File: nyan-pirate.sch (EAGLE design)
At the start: 40 parts, among them IC1 PIC24FJ64GA002, IC2 FT232RL, IC3 4066, J1 CON-USB-MINI-BUSB1

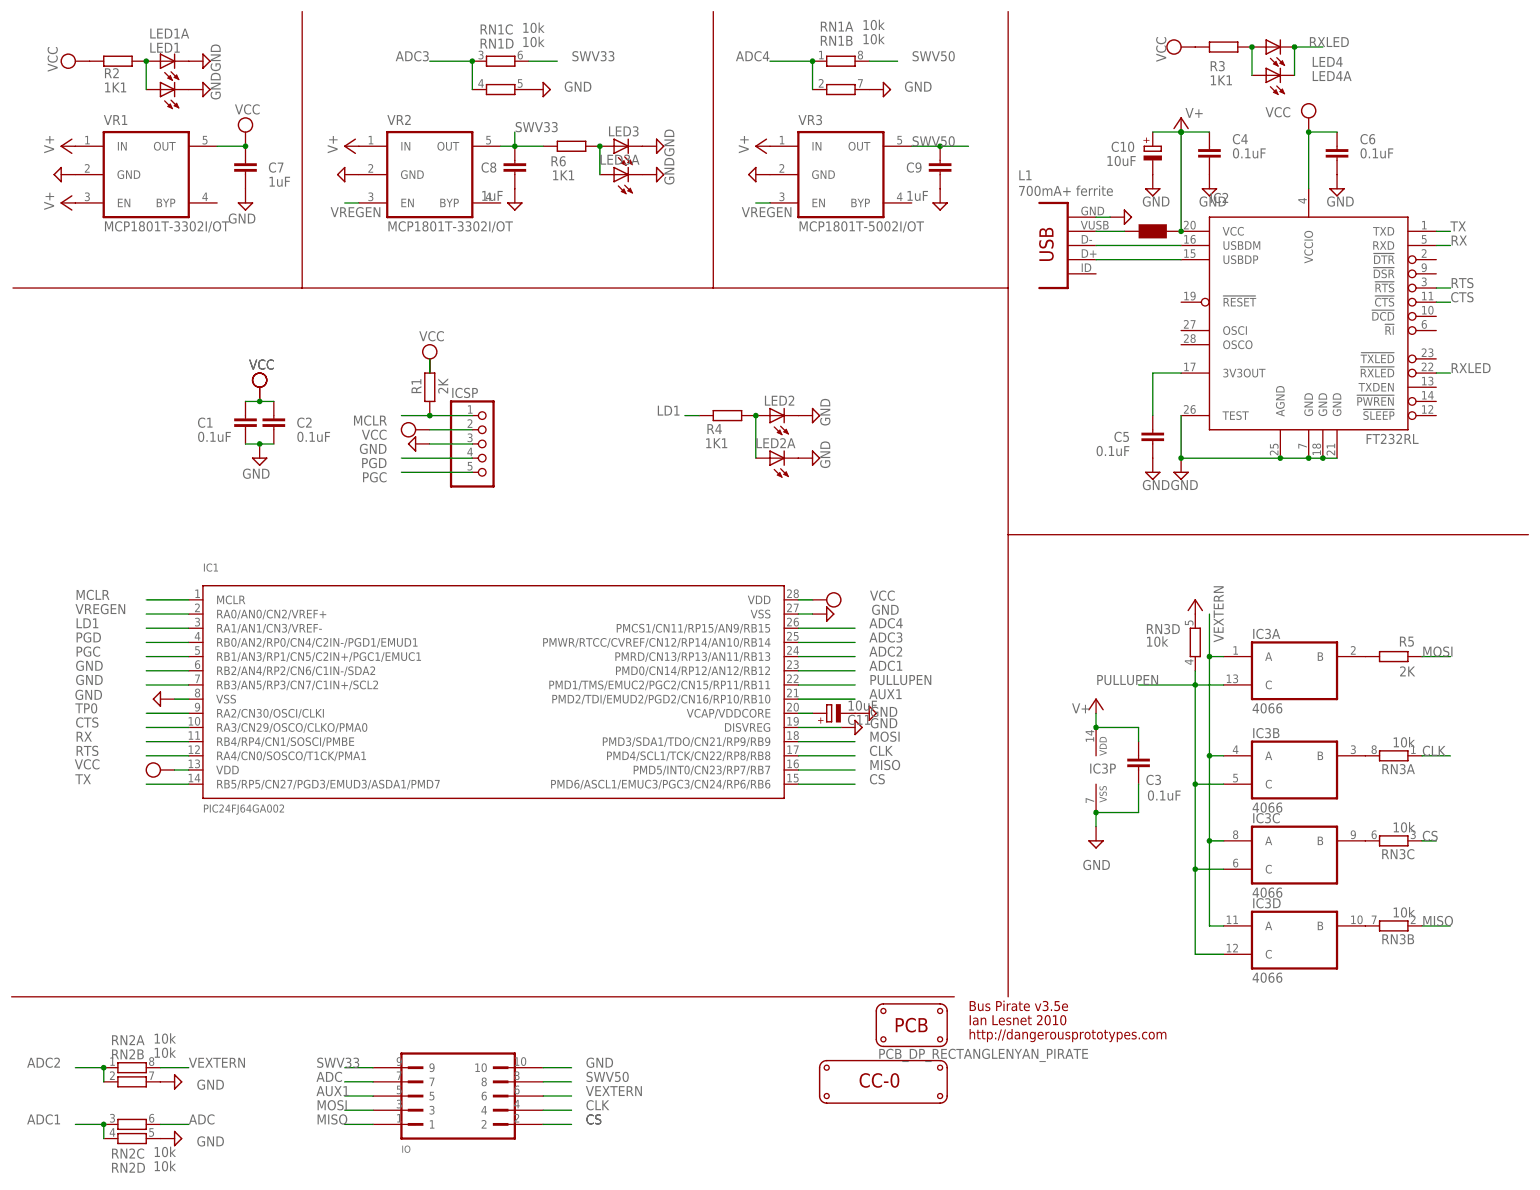
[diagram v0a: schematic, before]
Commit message: changes to make special Bsides PDX 2014 version
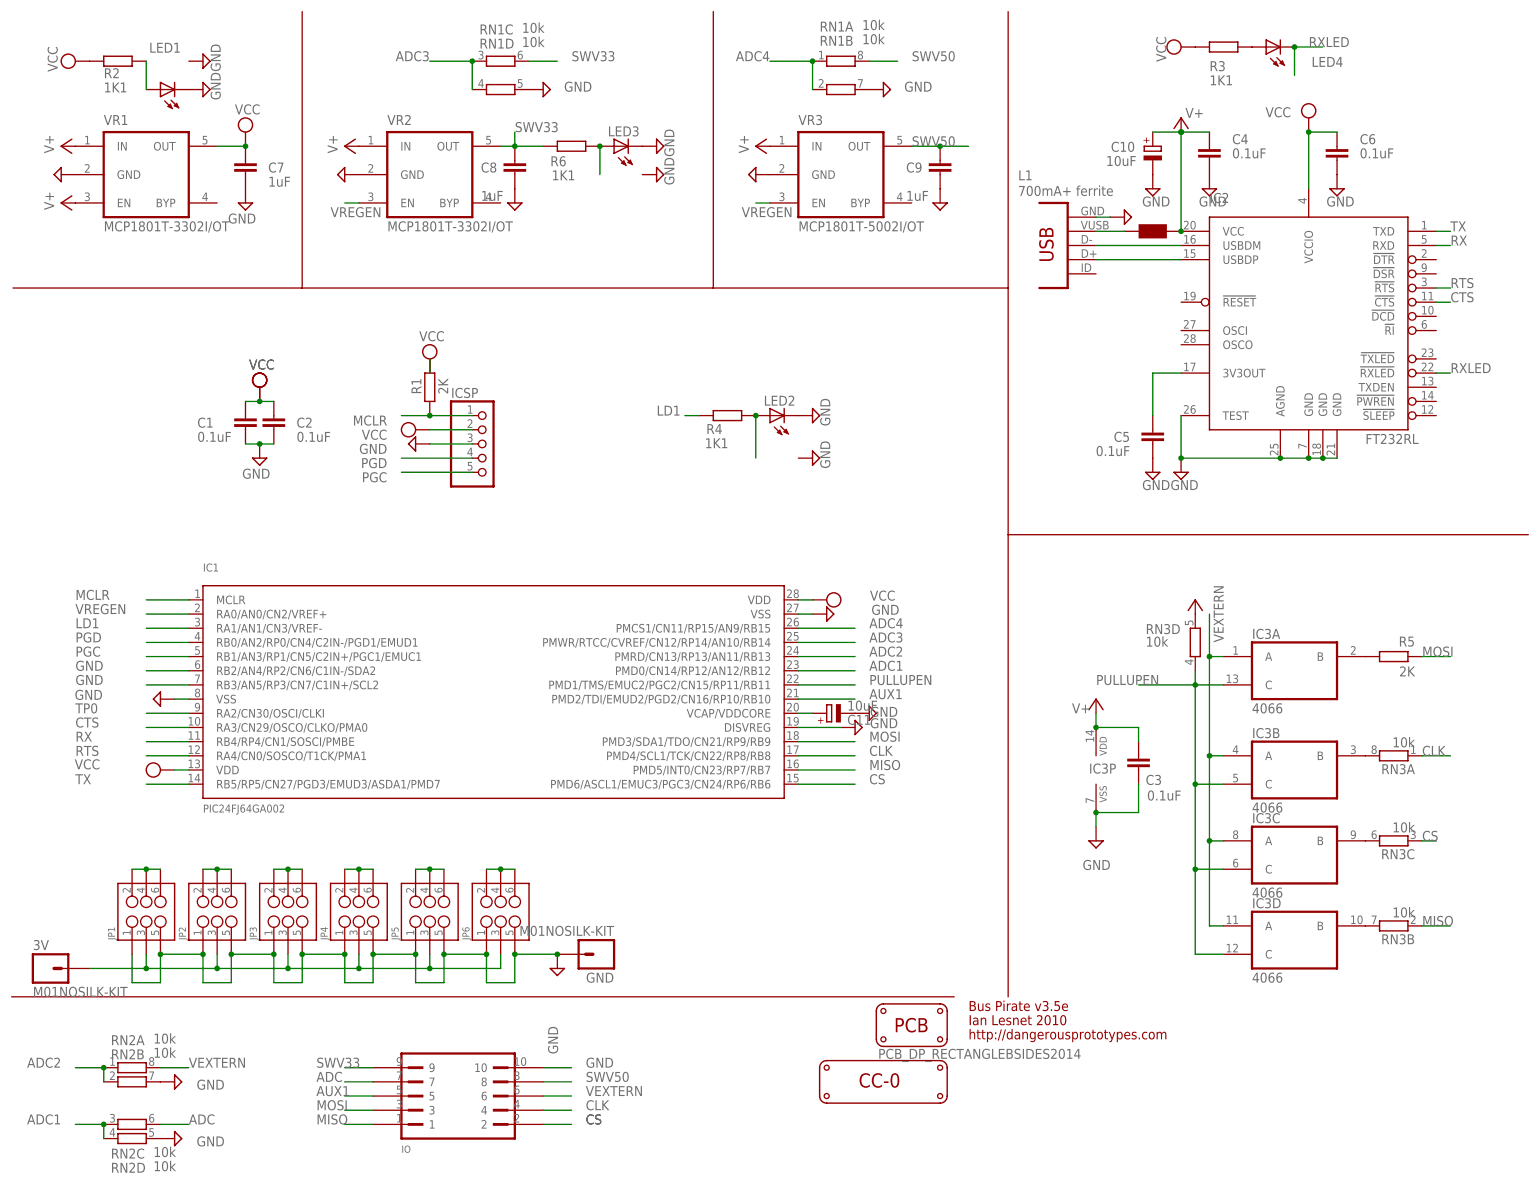
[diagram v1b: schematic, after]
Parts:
- removed LED1A, LED2A, LED3A, LED4A: (no value), led:LEDCHIP-LED0805
- added 3V, GND: M01NOSILK-KIT, SparkFun-Connectors:M01NOSILK-KIT
- added JP1, JP2, JP3, JP4, JP5, JP6: (no value), SparkFun-Connectors:M03X2NO_SILK
- PCB1: value PCB_DP_RECTANGLENYAN_PIRATE -> PCB_DP_RECTANGLEBSIDES2014; device dp_pcb:PCB_DP_RECTANGLENYAN_PIRATE -> dp_pcb:PCB_DP_RECTANGLEBSIDES2014
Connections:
- new net N$10: JP2.2, JP2.4, JP2.6
- new net N$11: JP3.2, JP3.4, JP3.6
- new net N$12: JP4.2, JP4.4, JP4.6
- new net N$14: JP5.2, JP5.4, JP5.6
- new net N$17: JP6.2, JP6.4, JP6.6
- new net N$20: 3V.1, JP1.3, JP2.3, JP3.3, JP4.3, JP5.3, JP6.3
- new net N$8: JP1.2, JP1.4, JP1.6
- net GND: now also GND.1, JP1.1, JP1.5, JP2.1, JP2.5, JP3.1, JP3.5, JP4.1, JP4.5, JP5.1, JP5.5, JP6.1, JP6.5; no longer LED1A.C, LED2A.C, LED3A.C
- net N$13: no longer LED4A.A
- net N$18: no longer LED3A.A
- net N$6: no longer LED2A.A
- net N$7: no longer LED1A.A
- net RXLED: no longer LED4A.C
